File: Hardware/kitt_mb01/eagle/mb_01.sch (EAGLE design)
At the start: 117 parts, among them IC2.0 BQ24266RGET, IC3.01 LSM9DS1, U1.01 RT8293A, U6.01 TPS61032RSARPSDO-G16, U7.01 SI1922EDH, U7.03 SI1922EDH, U7.2 SI1922EDH, X2.01 S2B-PH-K-S(LF)(SN), X7.02 ARDUINO_UNO, X7.03 CON_HEADER_1X02, X7.05 MOTOR, X7.06 CON_HEADER_1X02, X7.08 CON_HEADER_1X02, X7.09 0R-JUMPA, X7.10 0R-JUMPA, X7.11 CON_HEADER_1X02

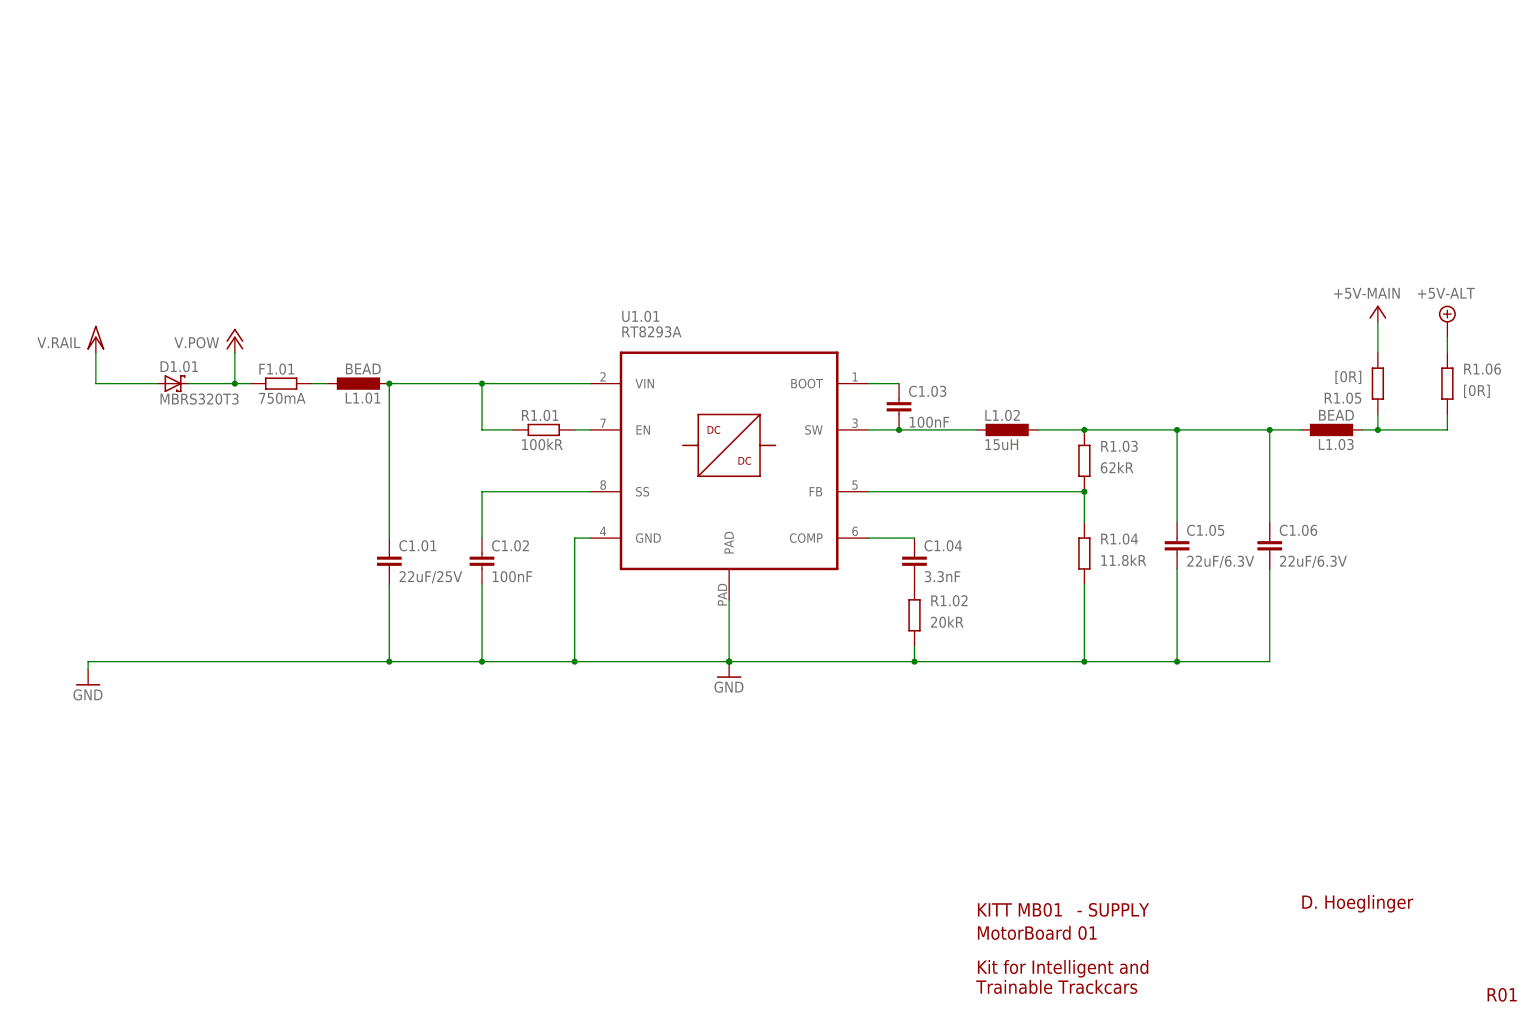
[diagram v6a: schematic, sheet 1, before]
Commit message: snapshot of mb01 board layout -> added 3V3 LDO regulator (neither ideal in placement nor routing, but w/e)
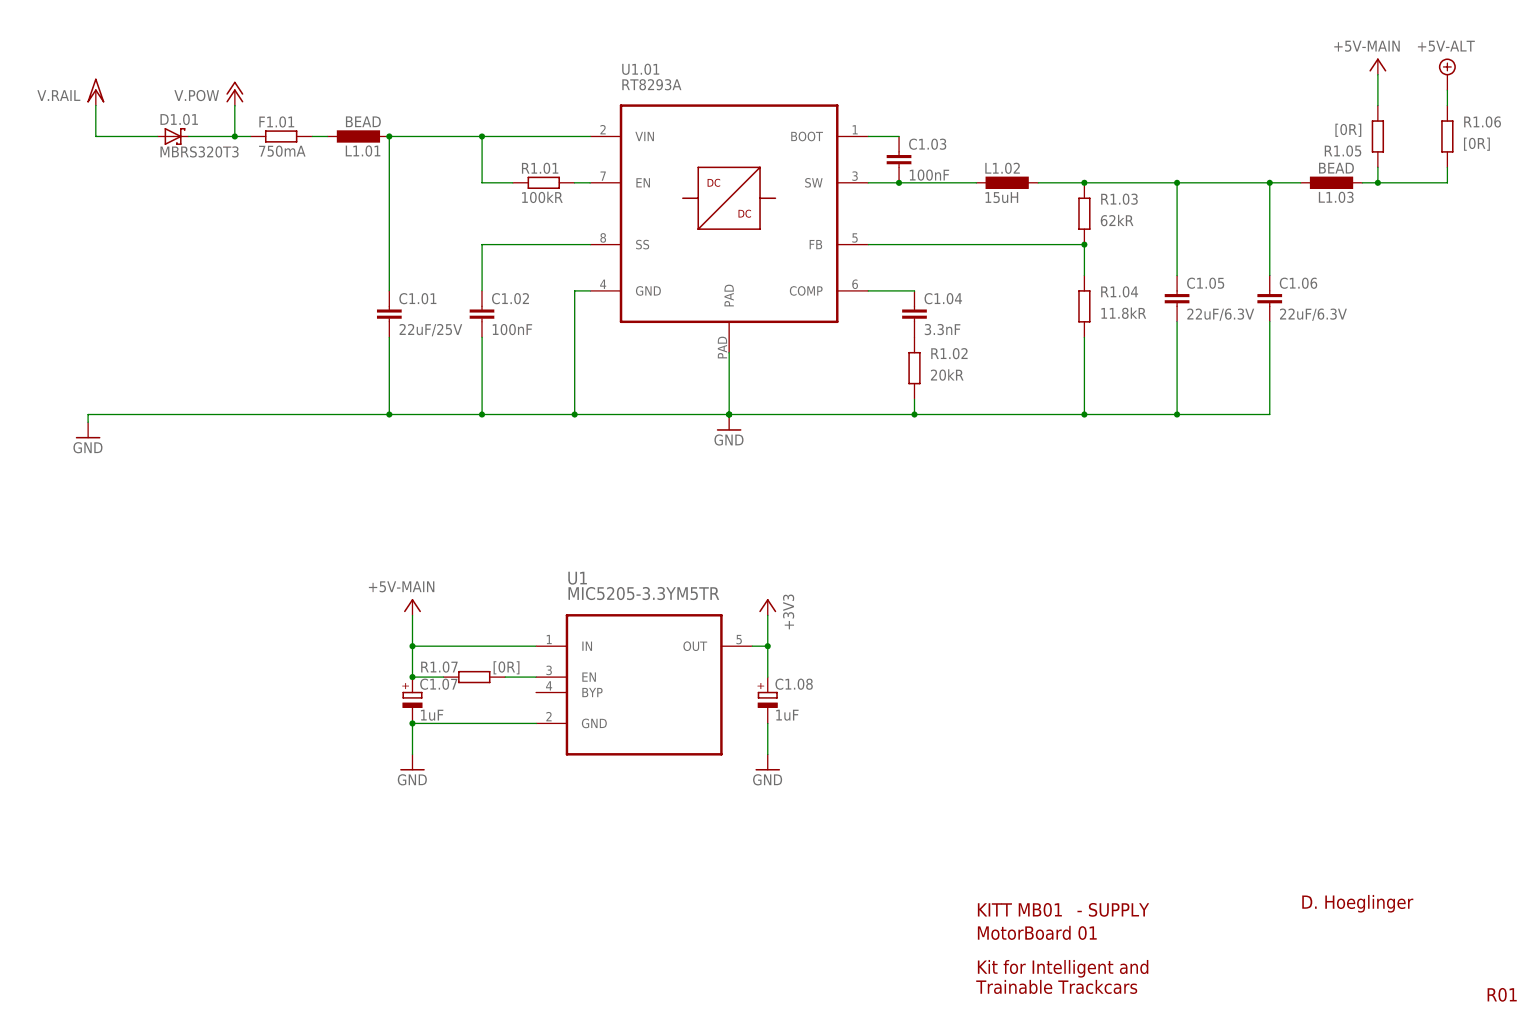
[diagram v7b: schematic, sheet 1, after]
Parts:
- added C1.07, C1.08: 1uF, rcl:CPOL-EUA/3216-18R
- added R1.07: [0R], rcl:R-EU_R0402
- added U1: MIC5205-3.3YM5TR, kitt.ic:MIC5205-3.3YM5TR
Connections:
- new net N$49: R1.07.1, U1.EN
- net +3V3: now also C1.08.+, U1.OUT
- net +5V: now also C1.07.+, R1.07.2, U1.IN
- net GND: now also C1.07.-, C1.08.-, U1.GND
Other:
- moved on the sheet: C1.01, C1.02, C1.03, C1.04, C1.05, C1.06, D1.01, F1.01, L1.01, L1.02, L1.03, R1.01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

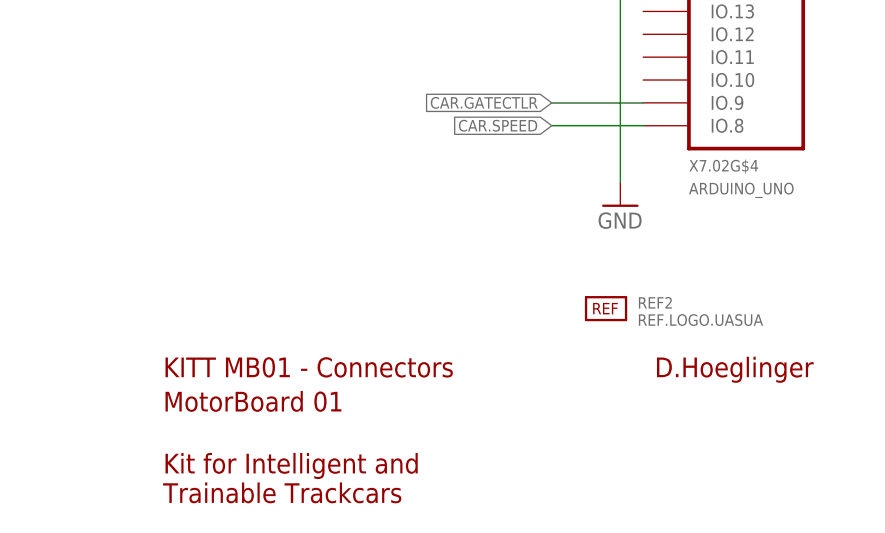
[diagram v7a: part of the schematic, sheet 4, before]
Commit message: added logos and text to bottom side
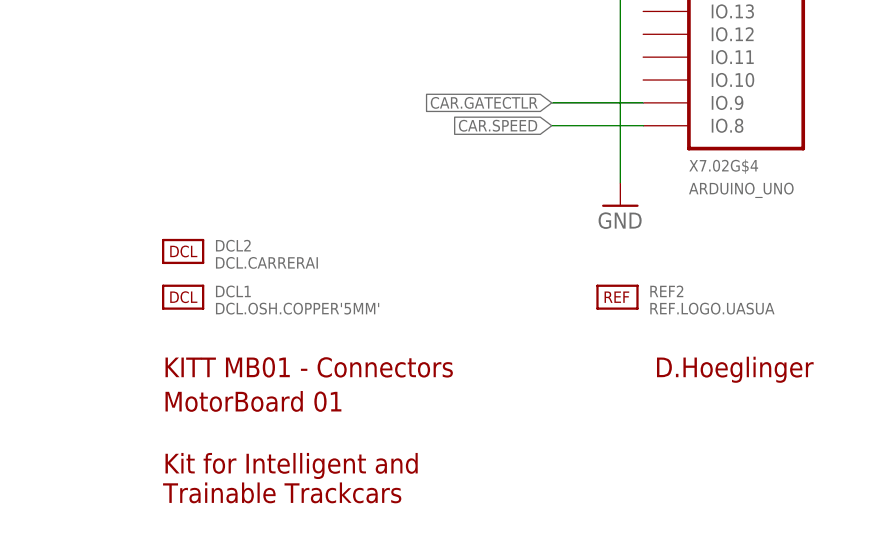
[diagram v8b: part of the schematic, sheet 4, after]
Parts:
- added DCL1: DCL.OSH.COPPER'5MM', kitt.refs:DCL.OSH.COPPER'5MM'
- added DCL2: DCL.CARRERAI, kitt.refs:DCL.CARRERAI
- renumbered U1 to U1.02
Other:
- moved on the sheet: REF2
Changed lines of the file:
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@@
 <part name="R7.10" library="rcl" deviceset="R-EU_" device="R0603" value="330R"/>
 <part name="GND27" library="supply1" deviceset="GND" device=""/>
-<part name="U1" library="kitt.ic" deviceset="MIC5205-3.3YM5TR" device=""/>
+<part name="U1.02" library="kitt.ic" deviceset="MIC5205-3.3YM5TR" device=""/>
 <part name="GND38" library="supply1" deviceset="GND" device=""/>
 <part name="P+5VMAIN7" library="supply1" deviceset="+5V" device="" value="+5V-MAIN"/>
@@
 <part name="GND39" library="supply1" deviceset="GND" device=""/>
 <part name="+3V7" library="supply1" deviceset="+3V3" device=""/>
+<part name="DCL1" library="kitt.refs" deviceset="DCL.OSH.COPPER" device="'5MM'"/>
+<part name="DCL2" library="kitt.refs" deviceset="DCL.CARRERAI" device=""/>
 </parts>
 <sheets>
@@
 </instance>
 <instance part="GND29" gate="1" x="17.78" y="97.79"/>
-<instance part="U1" gate="A" x="109.22" y="60.96"/>
+<instance part="U1.02" gate="A" x="109.22" y="60.96"/>
 <instance part="GND38" gate="1" x="71.12" y="43.18"/>
 <instance part="P+5VMAIN7" gate="1" x="71.12" y="71.12" smashed="yes" rot="MR0">
@@
 <segment>
 <pinref part="GND38" gate="1" pin="GND"/>
-<pinref part="U1" gate="A" pin="GND"/>
+<pinref part="U1.02" gate="A" pin="GND"/>
 <wire x1="71.12" y1="45.72" x2="71.12" y2="50.8" width="0.1524" layer="91"/>
 <wire x1="71.12" y1="50.8" x2="91.44" y2="50.8" width="0.1524" layer="91"/>
@@
 <segment>
 <pinref part="P+5VMAIN7" gate="1" pin="+5V"/>
-<pinref part="U1" gate="A" pin="IN"/>
+<pinref part="U1.02" gate="A" pin="IN"/>
 <wire x1="71.12" y1="68.58" x2="71.12" y2="63.5" width="0.1524" layer="91"/>
 <wire x1="71.12" y1="63.5" x2="91.44" y2="63.5" width="0.1524" layer="91"/>
@@
 <segment>
 <pinref part="R1.07" gate="G$1" pin="1"/>
-<pinref part="U1" gate="A" pin="EN"/>
+<pinref part="U1.02" gate="A" pin="EN"/>
 <wire x1="86.36" y1="58.42" x2="91.44" y2="58.42" width="0.1524" layer="91"/>
 </segment>
@@
 <net name="+3V3" class="0">
 <segment>
-<pinref part="U1" gate="A" pin="OUT"/>
+<pinref part="U1.02" gate="A" pin="OUT"/>
 <pinref part="C1.08" gate="G$1" pin="+"/>
 <wire x1="127" y1="63.5" x2="129.54" y2="63.5" width="0.1524" layer="91"/>
@@
 <instance part="D7.07" gate="G$1" x="93.345" y="134.62"/>
 <instance part="GND37" gate="1" x="93.345" y="121.285"/>
-<instance part="REF2" gate="G$1" x="209.55" y="26.67"/>
+<instance part="REF2" gate="G$1" x="210.82" y="27.94"/>
 <instance part="R7.05" gate="1" x="204.47" y="127" smashed="yes">
 <attribute name="NAME" x="194.945" y="127.2286" size="1.4224" layer="95"/>
@@
 <instance part="R7.10" gate="G$1" x="46.355" y="43.18" rot="R90"/>
 <instance part="GND27" gate="1" x="213.36" y="39.37"/>
+<instance part="DCL1" gate="G$1" x="162.56" y="27.94"/>
+<instance part="DCL2" gate="G$1" x="162.56" y="33.02"/>
 </instances>
 <busses>
